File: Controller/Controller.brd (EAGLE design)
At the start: 36.3 x 29.8 mm, 40 parts, among them Q1 16Mhz, Q2 DMMT5401, Q3 DMG2305UX

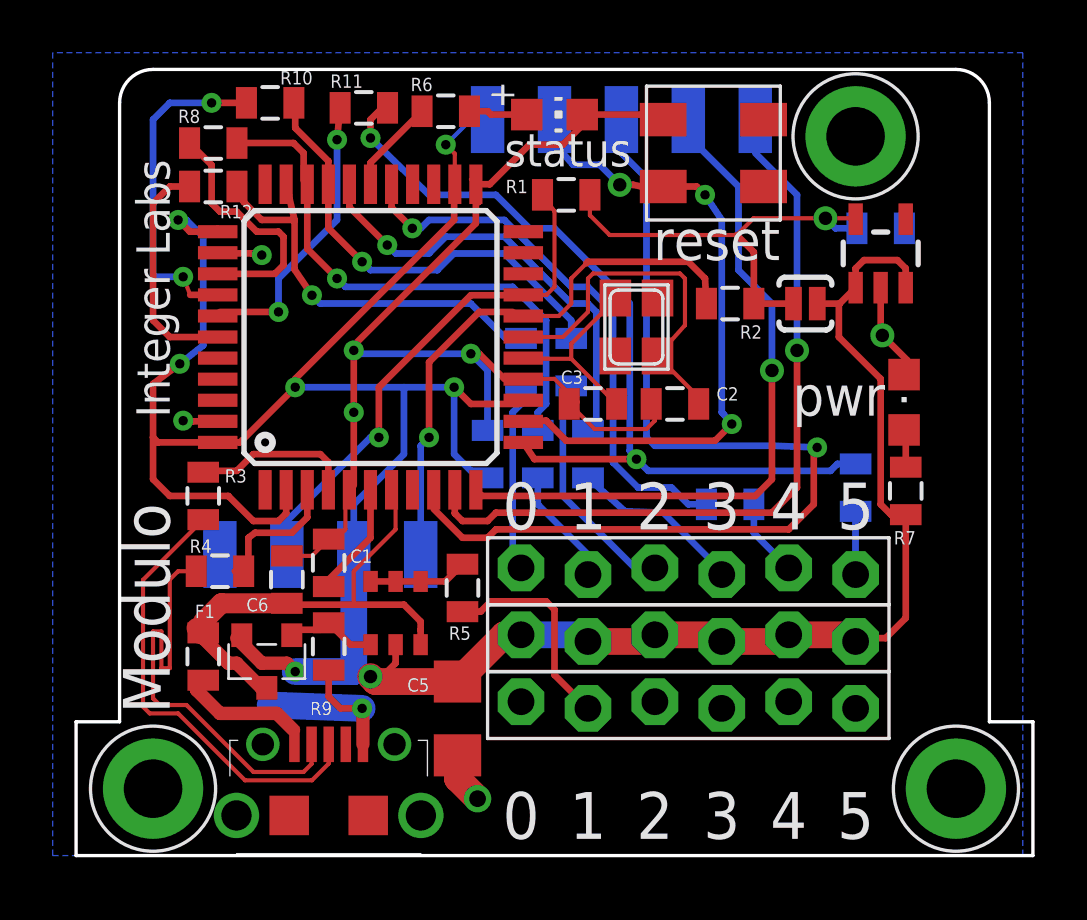
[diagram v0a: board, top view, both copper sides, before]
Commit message: Renamed 32u4 to Controller
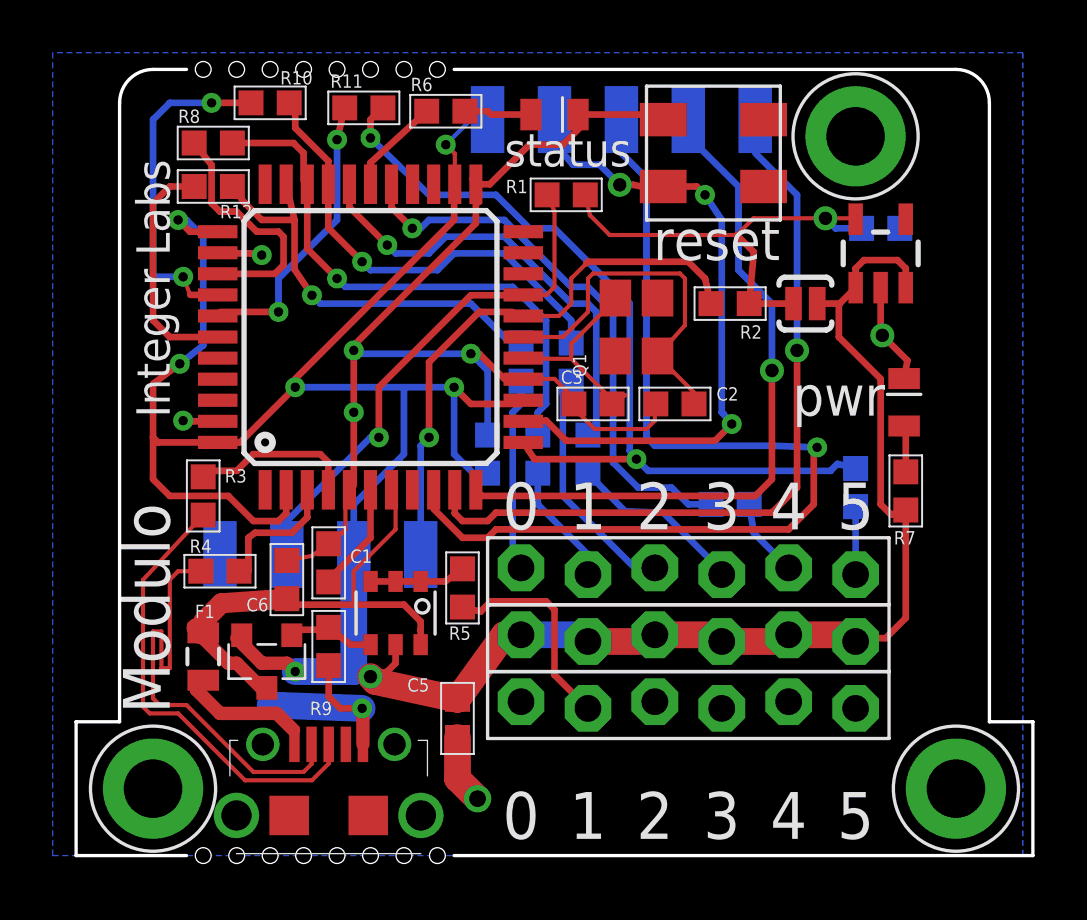
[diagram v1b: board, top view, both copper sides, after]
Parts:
- removed U$1: 3.3V/150mA, SparkFun-PowerIC:SOT23-5
- removed U$6: TACT-SWITCHBOURNS-7914J, IntegerLabs:BOURNS-7914J
- added SW1: blue, Modulo:BOURNS-7914J
- added U1: MIC5205-3.3YM5 TR, Modulo:SOT23-5
- C1, C2, C3, C6: device SparkFun-Capacitors:0805 -> Modulo:0603
- C4, C7: value .47uF -> 100nF; device SparkFun-Capacitors:0805 -> Modulo:0603
- C5: value 47uF -> 10uF; device SparkFun-Capacitors:1206 -> Modulo:0603
- F1: device SparkFun-Resistors:0805 -> Modulo:0805
- FOOTPRINT: value Controller -> DEVICE-PCB-TABS; device IntegerLabs:FOOTPRINT2 -> Modulo:DEVICE-PCB-TABS
- LED1: value (none) -> blue; device adafruit:CHIP-LED0805 -> Modulo:0805-LED
- LED2: value (none) -> blue; device led:CHIPLED_0805 -> Modulo:0805-LED
- Q1: device adafruit:NX3225 -> Modulo:NX3225
- R1, R10, R11, R12, R2, R8: value 2k -> 1.5KΩ; device SparkFun-Resistors:0805 -> Modulo:0603
- R13, R14, R15, R16, R17, R18: value 130 -> 150Ω; device SparkFun-Resistors:0805 -> Modulo:0603
- R3, R4: value 22 -> 22Ω; device SparkFun-Resistors:0805 -> Modulo:0603
- R5: value 10k 1% -> 10KΩ; device SparkFun-Passives:0805 -> Modulo:0603
- R6, R7: value 680 -> 681Ω; device SparkFun-Resistors:0805 -> Modulo:0603
- R9: value 47k 1% -> 47KΩ; device SparkFun-Passives:0805 -> Modulo:0603
- renumbered U$2 to U2, U$4 to U3
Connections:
- net +3.3V: now also U1.5; no longer U$1.5
- net G1: now also Q1.2; no longer Q1.4
- net G2: now also Q1.4; no longer Q1.2
- net GND: now also SW1.NEG$1, SW1.NEG$2, U1.2; no longer U$1.2, U$6.NEG$1
- net RESET: now also SW1.POS$1, SW1.POS$2; no longer U$6.POS$1
- net VCC: now also U1.1, U1.3; no longer U$1.1, U$1.3
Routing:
- net GND: track 70.0 -> 71.2 mm
- net VCC: track 114.2 -> 115.0 mm
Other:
- outline, holes or cut-outs redrawn

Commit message: Major revision of all boards. Cleaned up old files. Exported BOM csv files for all boards
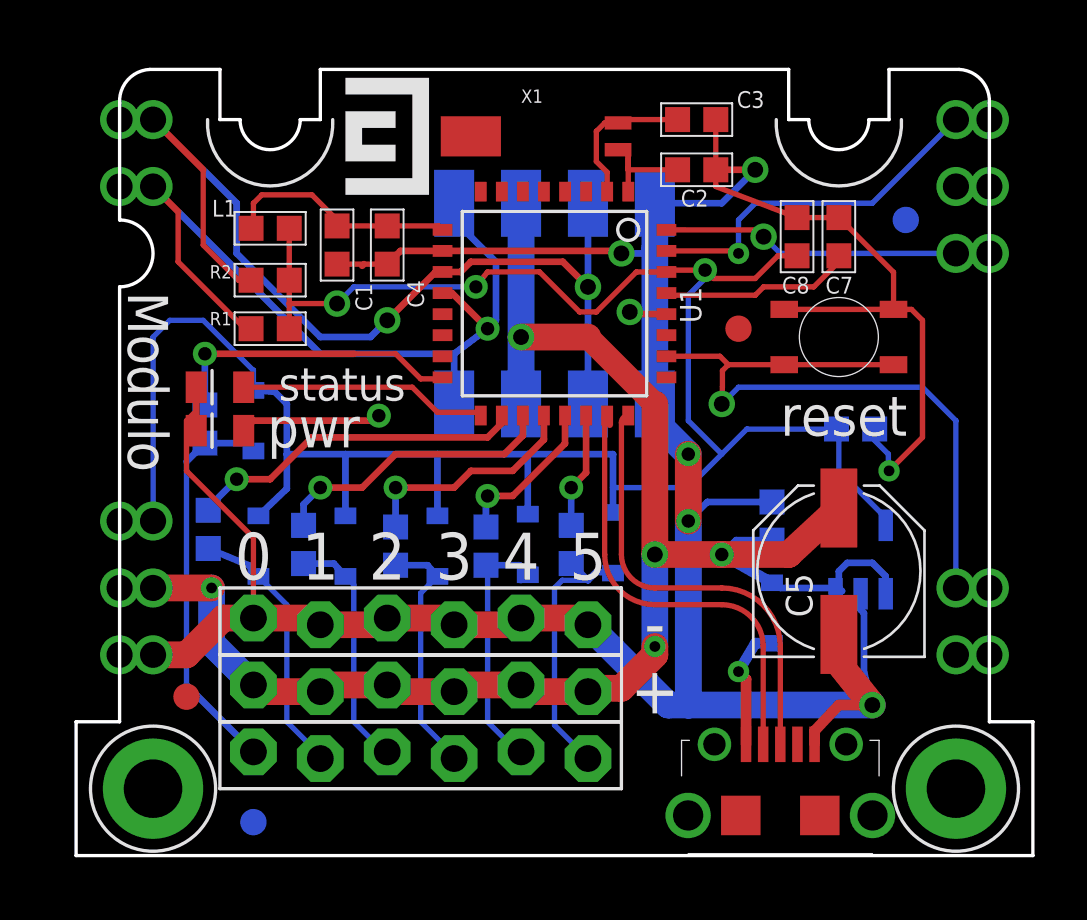
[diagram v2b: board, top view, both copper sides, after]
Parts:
- removed FOOTPRINT: DEVICE-PCB-TABS, Modulo:DEVICE-PCB-TABS
- removed Q1: 16Mhz, Modulo:NX3225
- removed Q2: DMMT5401, IntegerLabs:SOT-26
- removed Q3: DMG2305UX, transistor-power:MICRO3
- removed R10, R11, R12: 1.5KΩ, Modulo:0603
- removed R13, R14, R15, R16, R17, R18: 150Ω, Modulo:0603
- removed R9: 47KΩ, Modulo:0603
- removed SJ1: SOLDERJUMPERNO, SparkFun-Passives:SJ_2S-NO
- removed U3: USBFCI-MICROB, IntegerLabs:USB-MICROB-FCI
- added C8: .1uF, Modulo:0603
- added C9: 10uF, Modulo:0603
- added D1, D2, D3, D4, D5, D6, D7: DIODE-SCHOTTKY-BAT60A, Modulo:SOD-323
- added F2, F3, F4: FIDUCIAL, Modulo:FIDUCIAL_1MM
- added JP4, JP5: (no value), adafruit:1X06-BIGLOCK
- added L1: 10uH, Modulo:0603
- added PCB1: DEVICE-PCB, Modulo:DEVICE-PCB
- added U$1, U$2: (no value), Modulo:LOGO-SMALL
- added X1: CRYSTAL-AB26TRQ-32.768K, Modulo:CRYSTAL-AB26TRQ
- C1: value 1uF -> 10uF
- C4, C7: value 100nF -> .1uF
- C5: value 10uF -> 56uF; device Modulo:0603 -> Modulo:PANASONIC_D
- F1: value MF-PSMF110X-2 -> FIDUCIAL; device Modulo:0805 -> Modulo:FIDUCIAL_1MM
- JP1: value (none) -> USBFCI-MICROB; device adafruit:1X06-BIGLOCK -> Modulo:USB-MICROB-FCI
- JP2: value (none) -> HEADER-1X4-AMPMODU; device adafruit:1X06-BIGLOCK -> Modulo:AMPMODU-4P
- R1, R2: value 1.5KΩ -> 1KΩ
- R3, R4: value 22Ω -> 470Ω
- R5: value 10KΩ -> 470Ω
- R6, R7: value 681Ω -> 470Ω
- R8: value 1.5KΩ -> 470Ω
- SW1: value blue -> SWITCH-PTS-810; device Modulo:BOURNS-7914J -> Modulo:TACT-SWITCH-PTS-810
- U1: value MIC5205-3.3YM5 TR -> ATSAMD21E18A-AU; device Modulo:SOT23-5 -> Modulo:TQFP-32
- U2: value ATMEGA32U4TQFP -> MIC5205-3.3YM5 TR; device SparkFun-DigitalIC:SPARKFUN-DIGITALIC_TQFP44 -> Modulo:SOT23-5
- moved R7 26.5 mm to (4.64, 12.4), flipped to the bottom, turned to 270 degrees
- moved LED2 26.0 mm to (5.08, 17.8), turned to 90 degrees
- moved U2 20.4 mm to (29.4, 11.2), flipped to the bottom, turned to 0 degrees
- moved C6 18.5 mm to (26.0, 12.7), flipped to the bottom
- moved R2 17.5 mm to (6.99, 21.8)
- moved LED1 17.5 mm to (5.08, 16.1), turned to 90 degrees
- moved R6 17.3 mm to (8.26, 11.8), flipped to the bottom, turned to 270 degrees
- moved JP2 16.1 mm to (17.8, 21.0), flipped to the bottom
- moved C5 15.5 mm to (28.6, 10.8), turned to 90 degrees
- moved R3 14.1 mm to (18.4, 11.8), flipped to the bottom, turned to 270 degrees
- moved U1 12.5 mm to (17.8, 21.0), turned to 270 degrees
- moved R1 12.3 mm to (6.99, 20.0)
- moved C1 12.1 mm to (9.53, 23.2), turned to 270 degrees
- moved C3 11.5 mm to (23.2, 27.9)
- moved JP3 11.1 mm to (12.7, 3.81), turned to 180 degrees
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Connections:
- removed net D0: R12.2, R18.1, U2.32
- removed net D1: R17.1, R8.2, U2.31
- removed net D2: R10.2, R16.1, U2.30
- removed net D3: R15.1, U2.29
- removed net D4: R14.1, U2.27
- removed net D5: R11.2, R13.1, U2.12
- removed net G1: Q1.2
- removed net G2: Q1.4
- removed net MISO: FOOTPRINT.PROG3, U2.11
- removed net MOSI: FOOTPRINT.PROG4, U2.10
- removed net N$1: C1.1, U2.6
- removed net N$10: R10.1, U2.37
- removed net N$11: R8.1, U2.36
- removed net N$12: LED2.A, R7.2
- removed net N$14: Q2.1, Q2.2, Q2.3, R5.2
- removed net N$15: C2.1, Q1.1, U2.17
- removed net N$16: Q2.4, Q3.1, R9.2
- removed net N$4: C3.1, Q1.3, U2.16
- removed net N$5: LED1.A, R6.2
- removed net N$8: R3.2, U2.4
- removed net N$9: R4.2, U2.3
- removed net SCK: FOOTPRINT.PROG2, U2.9
- removed net VBUS: C6.1, F1.2, Q2.6, Q3.3, U2.7
- new net IO0: R8.1, U1.16
- new net IO1: R7.1, U1.18
- new net IO2: R6.1, U1.19
- new net IO3: R5.1, U1.20
- new net IO4: R4.1, U1.21
- new net IO5: R3.1, U1.22
- new net N$21: C1.1, C4.1, L1.2, U1.9
- new net N$22: C7.1, U1.29
- new net SWCLK: PCB1.CLK, U1.31
- new net SWDIO: PCB1.SWDIO, U1.32
- net +3.3V: now also C8.1, C9.1, D2.C, D3.C, D4.C, D5.C, D6.C, D7.C, L1.1, LED1.A, PCB1.VPROG, U1.30, U2.5; no longer C7.1, SJ1.2, U1.5
- net D+: now also JP1.P3, U1.24; no longer R3.1, U3.P3
- net D-: now also JP1.P2, U1.23; no longer R4.1, U3.P2
- net GND: now also C2.1, C3.1, C5.-, C8.2, C9.2, JP1.P5, JP2.P$1, JP2.P$2, JP4.1, JP4.2, JP4.3, JP4.4, JP4.5, JP4.6, PCB1.GND, SW1.P$3, SW1.P$4, U1.10, U1.28, U2.2; no longer C2.2, C3.2, C5.2, FOOTPRINT.BUS0, JP2.1, JP2.2, JP2.3, JP2.4, JP2.5, JP2.6, R5.1, R9.1, SW1.NEG$1, SW1.NEG$2, U1.2, U2.15, U2.23, U2.35, U2.43, U2.5, U3.P5
- net LED: now also LED2.A, U1.17; no longer R6.1, U2.28
- net N$13: now also D3.A, JP3.2, R4.2; no longer JP1.2, R14.2
- net N$17: now also D4.A, JP3.3, R5.2; no longer JP1.3, R15.2
- net N$18: now also D5.A, JP3.4, R6.2; no longer JP1.4, R16.2
- net N$19: now also D6.A, JP3.5, R7.2; no longer JP1.5, R17.2
- net N$2: now also D2.A, JP3.1, R3.2; no longer JP1.1, R13.2
- net N$20: now also D7.A, JP3.6, R8.2; no longer JP1.6, R18.2
- net N$3: now also D1.A, JP1.P1; no longer F1.1, U3.P1
- net N$6: now also C2.2, U1.1, X1.XOUT; no longer R12.1, U2.39
- net N$7: now also C3.2, U1.2, X1.XIN; no longer R11.1, U2.38
- net RESET: now also PCB1.RESET, SW1.P$1, SW1.P$2, U1.26; no longer FOOTPRINT.PROG1, SW1.POS$1, SW1.POS$2, U2.13
- net SCL: now also JP2.P$7, JP2.P$8, PCB1.SCL, R1.2, U1.12; no longer FOOTPRINT.BUS3, R2.2, U2.18
- net SDA: now also JP2.P$3, JP2.P$4, PCB1.SDA, R2.2, U1.11; no longer FOOTPRINT.BUS1, R1.2, U2.19
- net VCC: now also C5.+, C6.1, D1.C, JP2.P$5, JP2.P$6, JP5.1, JP5.2, JP5.3, JP5.4, JP5.5, JP5.6, PCB1.VCC, U2.1, U2.3; no longer C4.1, C5.1, FOOTPRINT.BUS2, FOOTPRINT.PROG0, JP3.1, JP3.2, JP3.3, JP3.4, JP3.5, JP3.6, Q2.5, Q3.2, R7.1, SJ1.1, U1.1, U1.3, U2.14, U2.2, U2.24, U2.34, U2.44
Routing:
- net +3.3V: track 17.6 -> 96.4 mm, vias 1 -> 4
- net VCC: track 115.0 -> 65.1 mm, vias 7 -> 5
- net GND: track 71.2 -> 120.9 mm, vias 8 -> 7
- net SCK: track 37.4 -> 0.00 mm, vias 1 -> 0
- net D5: track 33.0 -> 0.00 mm, vias 2 -> 0
- net MOSI: track 29.2 -> 0.00 mm, vias 1 -> 0
- net MISO: track 26.8 -> 0.00 mm, vias 1 -> 0
- net D4: track 21.3 -> 0.00 mm, vias 1 -> 0
- net D1: track 21.2 -> 0.00 mm, vias 1 -> 0
- net VBUS: track 19.4 -> 0.00 mm
- net SDA: track 19.8 -> 38.2 mm, vias 1 -> 2
- net D2: track 17.6 -> 0.00 mm, vias 1 -> 0
- net D3: track 17.2 -> 0.00 mm, vias 1 -> 0
- net D0: track 16.0 -> 0.00 mm, vias 1 -> 0
- net SWCLK: track 0.00 -> 13.9 mm, vias 0 -> 1
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- removed copper zone on layer 16, net GND
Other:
- outline, holes or cut-outs redrawn
- board text added: "+"
- board text added: "-"

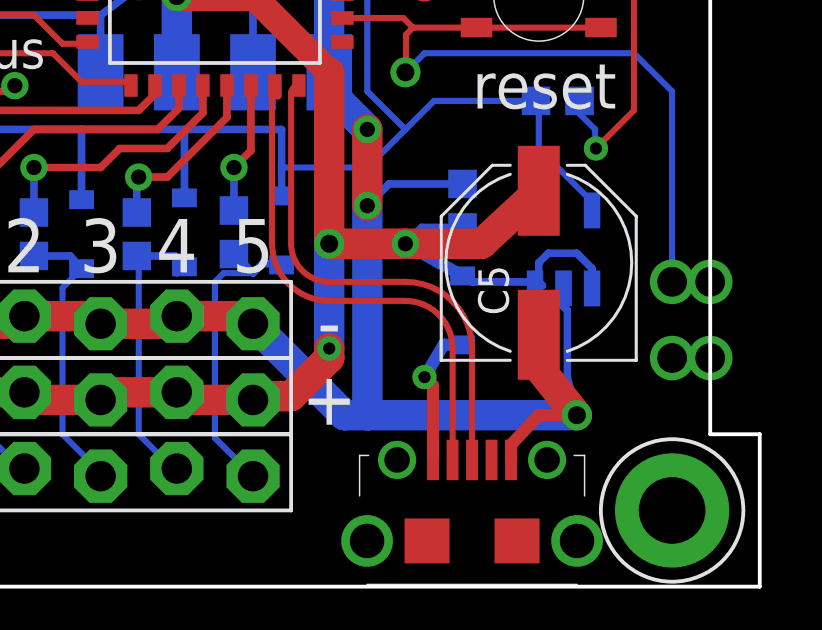
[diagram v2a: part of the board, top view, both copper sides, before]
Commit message: New diode selections
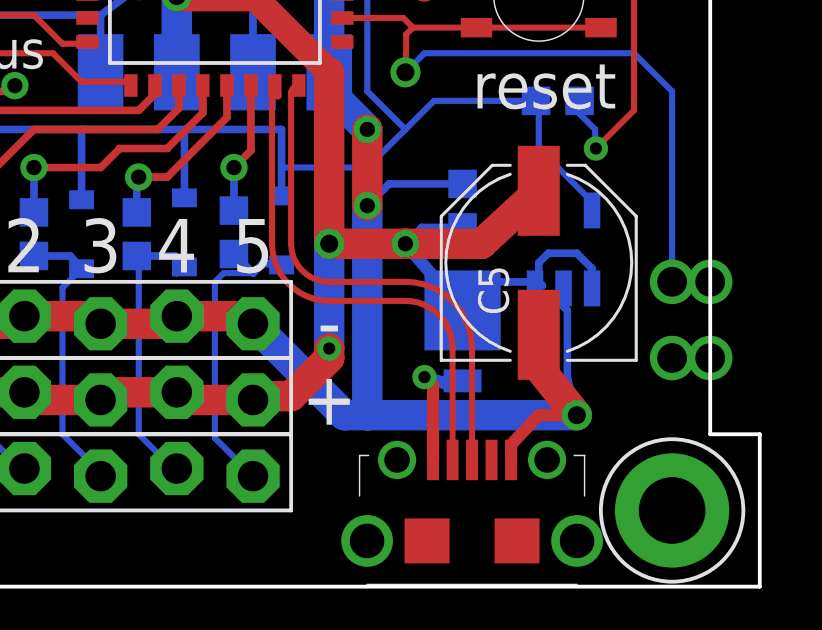
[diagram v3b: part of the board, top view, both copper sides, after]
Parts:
- D1: value DIODE-SCHOTTKY-BAT60A -> DIODE-SCHOTTKY; device Modulo:SOD-323 -> Modulo:SMP
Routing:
- net VCC: track 65.1 -> 66.5 mm
- net N$3: track 4.76 -> 4.18 mm
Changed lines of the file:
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@@
 <element name="D2" library="Modulo" package="SOD-323" value="DIODE-SCHOTTKY-BAT60A" x="20.0025" y="11.8745" smashed="yes" rot="MR270">
 <attribute name="NAME" x="20.463" y="14.562" size="0.508" layer="26" rot="MR270"/>
-<attribute name="PARTNUM" value="BAT60A" x="20.0025" y="11.8745" size="1.778" layer="28" rot="MR270" display="off"/>
+<attribute name="PARTNUM" value="CUS520,H3F" x="20.0025" y="11.8745" size="1.778" layer="28" rot="MR270" display="off"/>
 </element>
 <element name="D3" library="Modulo" package="SOD-323" value="DIODE-SCHOTTKY-BAT60A" x="16.764" y="11.811" smashed="yes" rot="MR270">
 <attribute name="NAME" x="17.102" y="13.446" size="0.508" layer="26" rot="MR0"/>
-<attribute name="PARTNUM" value="BAT60A" x="16.764" y="11.811" size="1.778" layer="28" rot="MR270" display="off"/>
+<attribute name="PARTNUM" value="CUS520,H3F" x="16.764" y="11.811" size="1.778" layer="28" rot="MR270" display="off"/>
 </element>
 <element name="D4" library="Modulo" package="SOD-323" value="DIODE-SCHOTTKY-BAT60A" x="13.335" y="11.7475" smashed="yes" rot="MR270">
 <attribute name="NAME" x="13.673" y="13.319" size="0.508" layer="26" rot="MR0"/>
-<attribute name="PARTNUM" value="BAT60A" x="13.335" y="11.7475" size="1.778" layer="28" rot="MR270" display="off"/>
+<attribute name="PARTNUM" value="CUS520,H3F" x="13.335" y="11.7475" size="1.778" layer="28" rot="MR270" display="off"/>
 </element>
 <element name="D5" library="Modulo" package="SOD-323" value="DIODE-SCHOTTKY-BAT60A" x="9.8425" y="11.7475" smashed="yes" rot="MR270">
 <attribute name="NAME" x="10.371" y="13.319" size="0.508" layer="26" rot="MR0"/>
-<attribute name="PARTNUM" value="BAT60A" x="9.8425" y="11.7475" size="1.778" layer="28" rot="MR270" display="off"/>
+<attribute name="PARTNUM" value="CUS520,H3F" x="9.8425" y="11.7475" size="1.778" layer="28" rot="MR270" display="off"/>
 </element>
 <element name="D6" library="Modulo" package="SOD-323" value="DIODE-SCHOTTKY-BAT60A" x="6.5405" y="11.7475" smashed="yes" rot="MR270">
 <attribute name="NAME" x="6.942" y="13.319" size="0.508" layer="26" rot="MR0"/>
-<attribute name="PARTNUM" value="BAT60A" x="6.5405" y="11.7475" size="1.778" layer="28" rot="MR270" display="off"/>
+<attribute name="PARTNUM" value="CUS520,H3F" x="6.5405" y="11.7475" size="1.778" layer="28" rot="MR270" display="off"/>
 </element>
 <element name="D7" library="Modulo" package="SOD-323" value="DIODE-SCHOTTKY-BAT60A" x="6.35" y="16.51" smashed="yes" rot="MR270">
 <attribute name="NAME" x="6.688" y="18.145" size="0.508" layer="26" rot="MR0"/>
-<attribute name="PARTNUM" value="BAT60A" x="6.35" y="16.51" size="1.778" layer="28" rot="MR270" display="off"/>
-</element>
-<element name="D1" library="Modulo" package="SOD-323" value="DIODE-SCHOTTKY-BAT60A" x="26.035" y="9.2075" smashed="yes" rot="MR270">
-<attribute name="PARTNUM" value="BAT60A" x="26.035" y="9.2075" size="1.778" layer="28" rot="MR270" display="off"/>
-<attribute name="NAME" x="25.019" y="10.0965" size="0.4064" layer="26" rot="MR270"/>
+<attribute name="PARTNUM" value="CUS520,H3F" x="6.35" y="16.51" size="1.778" layer="28" rot="MR270" display="off"/>
+</element>
+<element name="D1" library="Modulo" package="SMP" value="DIODE-SCHOTTKY" x="26.035" y="9.2075" smashed="yes" rot="MR270">
+<attribute name="PARTNUM" value="SS3P3-M3/84A" x="26.035" y="9.2075" size="1.778" layer="28" rot="MR270" display="off"/>
+<attribute name="NAME" x="24.384" y="8.8265" size="0.4064" layer="26" rot="MR270"/>
 </element>
 <element name="C5" library="Modulo" package="PANASONIC_D" value="56uF" x="28.575" y="10.795" rot="R90">
@@
 <wire x1="21.59" y1="17.145" x2="21.59" y2="11.43" width="1.016" layer="1"/>
 <contactref element="D1" pad="C"/>
-<wire x1="26.035" y1="10.3575" x2="26.3525" y2="10.16" width="0.254" layer="16"/>
+<wire x1="26.035" y1="9.2075" x2="26.3525" y2="10.16" width="0.254" layer="16"/>
 <wire x1="26.3525" y1="10.16" x2="28.575" y2="10.16" width="0.254" layer="16"/>
 <wire x1="28.575" y1="10.16" x2="28.695" y2="10.04" width="0.254" layer="16"/>
 <wire x1="28.695" y1="10.04" x2="28.3499" y2="10.04" width="0.254" layer="16"/>
 <wire x1="28.3499" y1="10.04" x2="28.4505" y2="9.9394" width="0.254" layer="16"/>
-<wire x1="24.13" y1="11.43" x2="26.035" y2="10.3575" width="0.4064" layer="16"/>
+<wire x1="24.13" y1="11.43" x2="26.035" y2="9.2075" width="0.4064" layer="16"/>
 <contactref element="C5" pad="+"/>
 <wire x1="24.13" y1="11.43" x2="26.67" y2="11.43" width="1.016" layer="1"/>
@@
 <wire x1="25.0525" y1="6.6975" x2="24.765" y2="6.985" width="0.4064" layer="1"/>
 <via x="24.765" y="6.985" extent="1-16" drill="0.4064"/>
-<wire x1="24.765" y1="6.985" x2="25.407" y2="8.0645" width="0.4064" layer="16"/>
-<wire x1="25.407" y1="8.0645" x2="26.035" y2="8.0575" width="0.4064" layer="16"/>
+<wire x1="24.765" y1="6.985" x2="25.407" y2="6.7945" width="0.4064" layer="16"/>
+<wire x1="25.407" y1="6.7945" x2="26.035" y2="6.858" width="0.4064" layer="16"/>
 </signal>
 </signals>
